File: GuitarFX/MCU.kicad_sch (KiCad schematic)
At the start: 36 parts, among them J2 USB_C_Receptacle_USB2.0, J301 Conn_ARM_SWD_TagConnect_TC2030, U2 STM32H733VGTx, U301 USBLC6-2SC6, Y301 24MHz

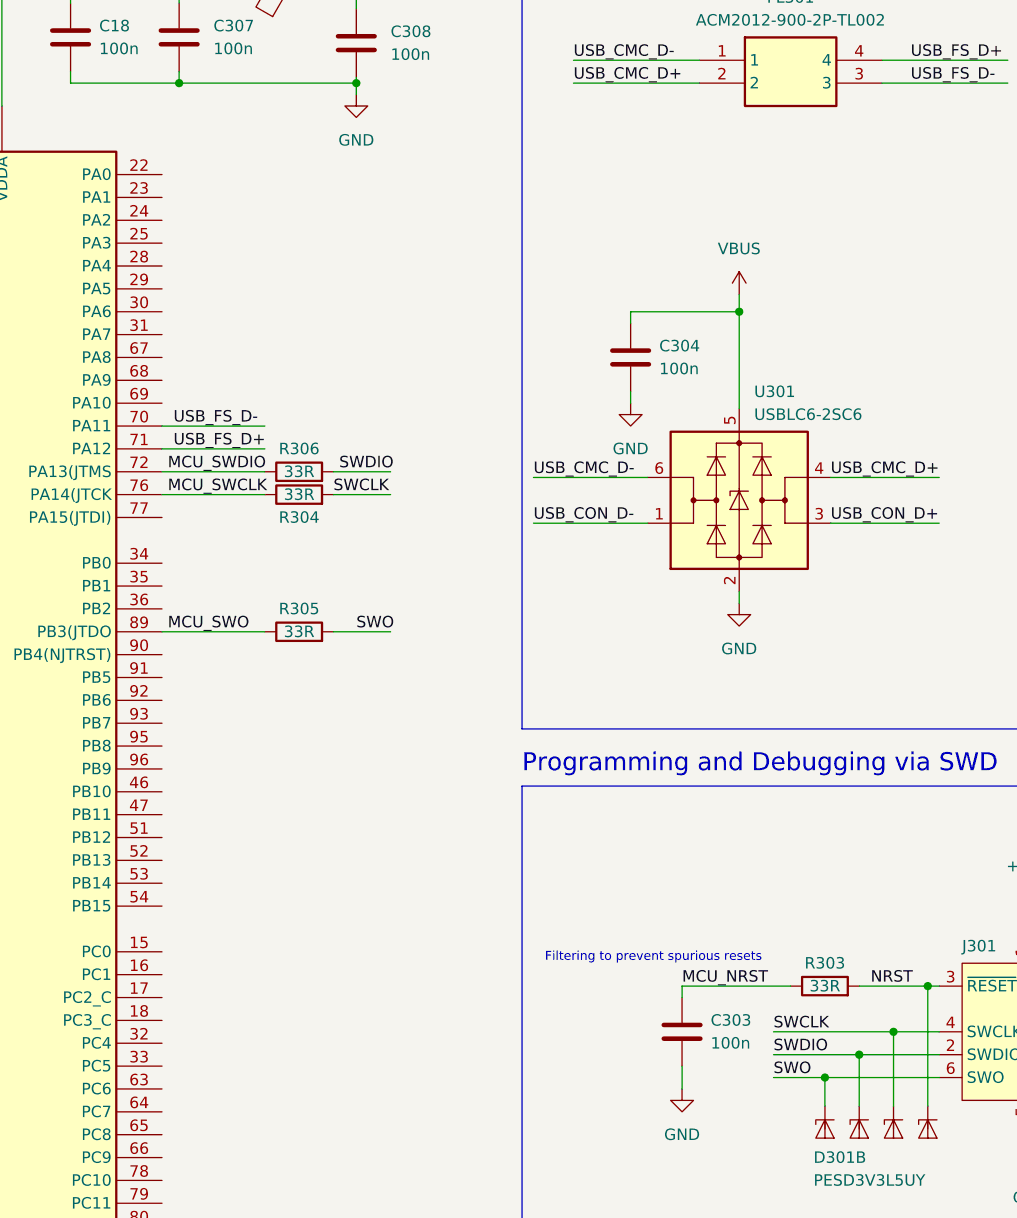
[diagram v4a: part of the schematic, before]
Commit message: Finished i2s and i2c connections on codec and mcu
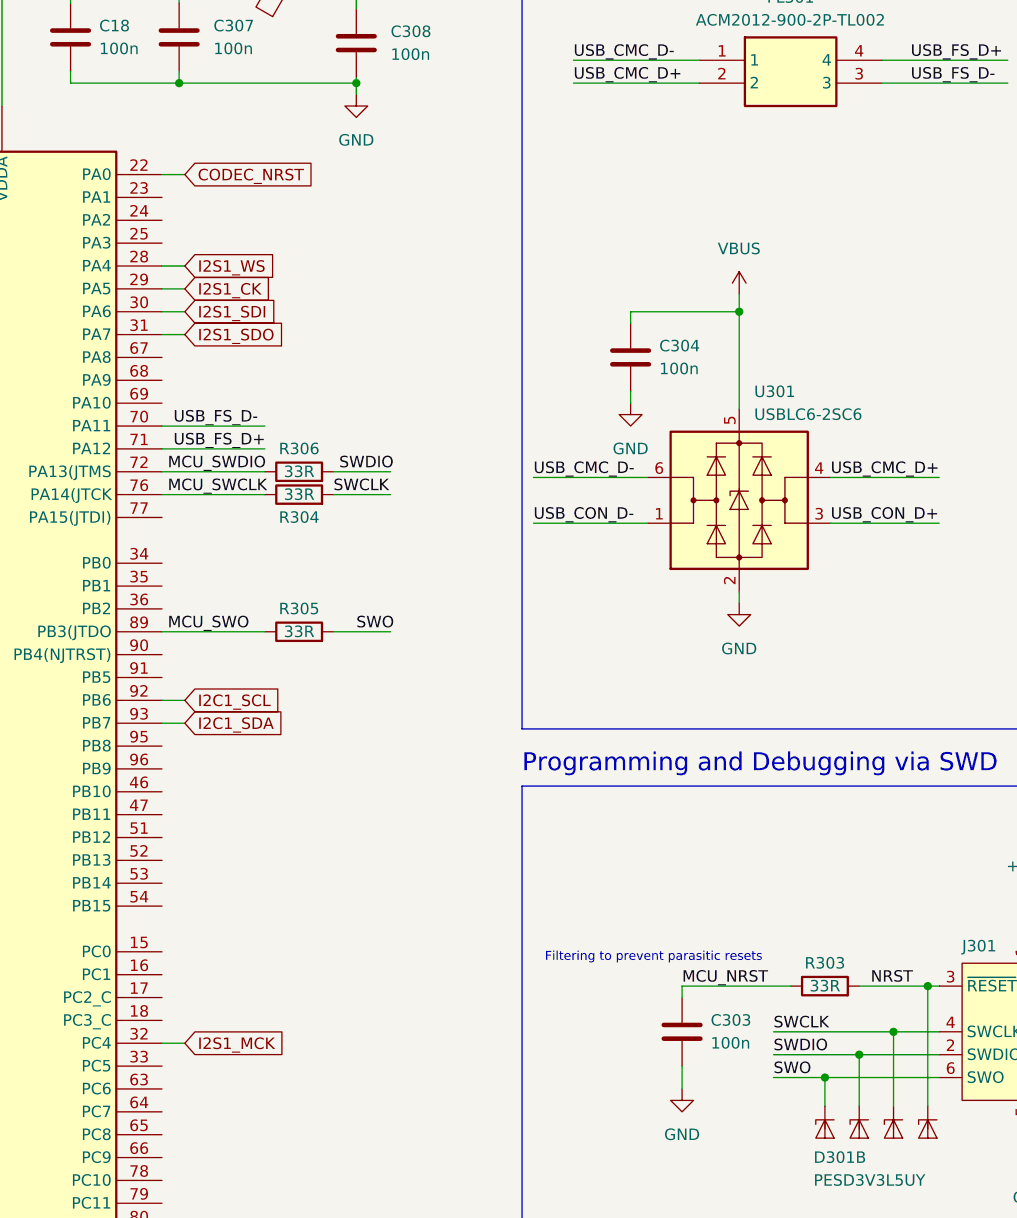
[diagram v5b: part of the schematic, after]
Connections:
- net CODEC_NRST: now reaches U2.22 (PA0)
- net I2S1_WS: now reaches U2.28 (PA4)
- net I2S1_CK: now reaches U2.29 (PA5)
- net I2S1_SDI: now reaches U2.30 (PA6)
- net I2S1_SDO: now reaches U2.31 (PA7)
- net I2S1_MCK: now reaches U2.32 (PC4)
- net I2C1_SCL: now reaches U2.92 (PB6)
- net I2C1_SDA: now reaches U2.93 (PB7)
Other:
- note added: "Filtering to prevent parasitic resets"
- note removed: "Filtering to prevent spurious resets"

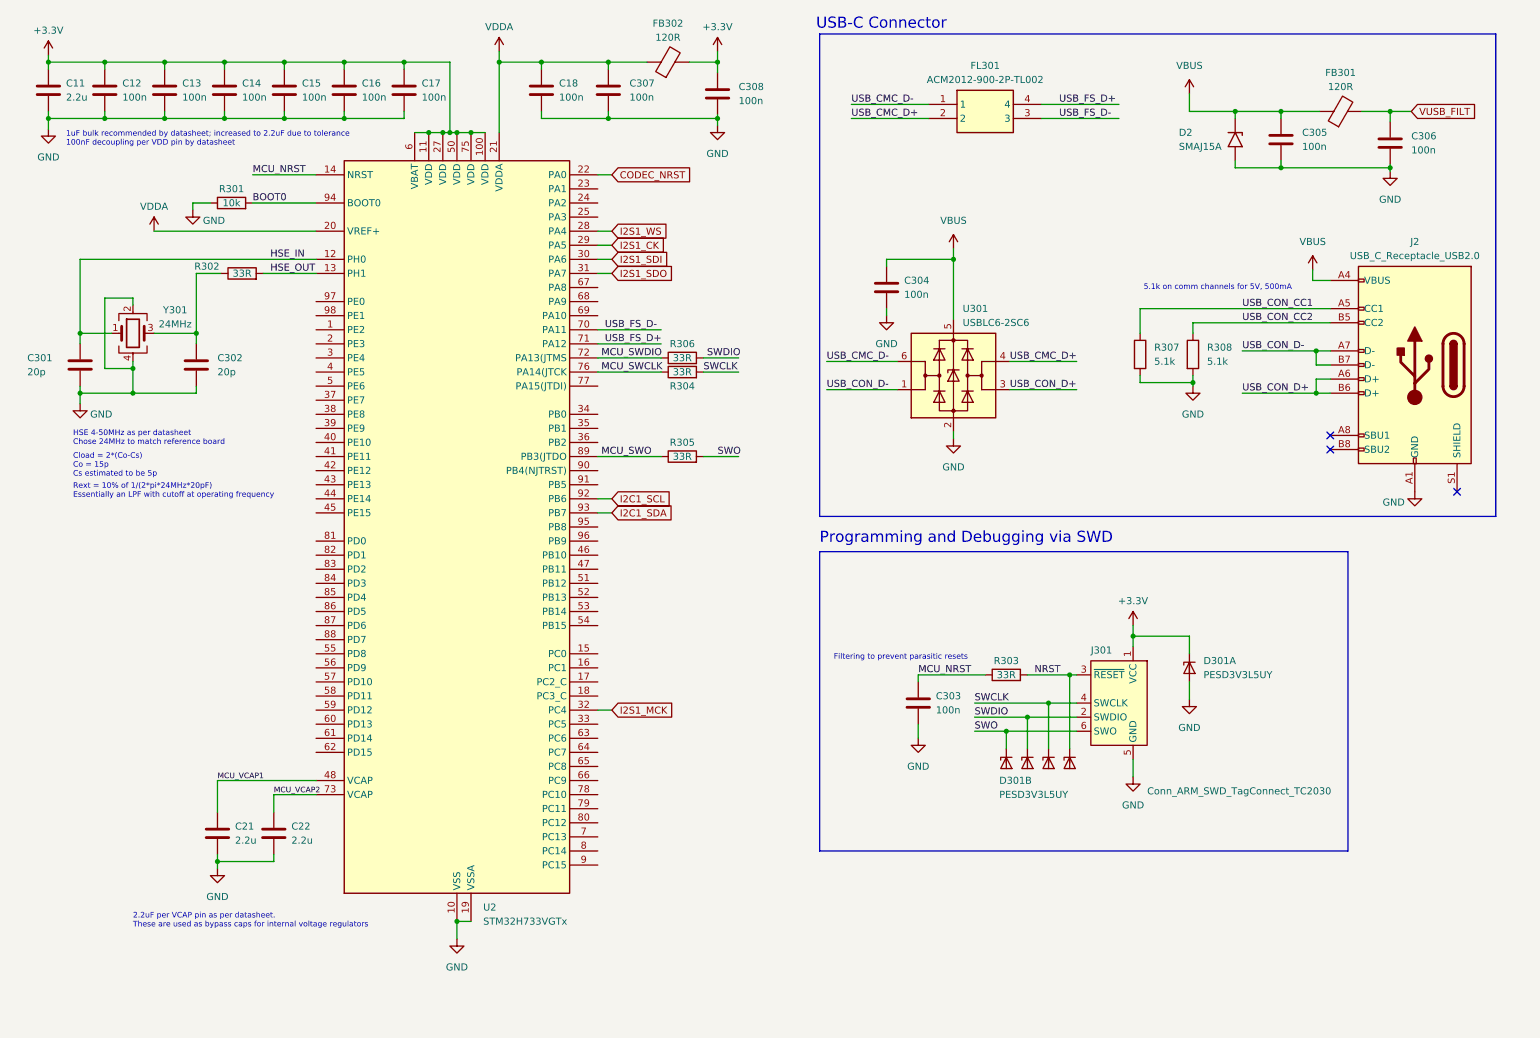
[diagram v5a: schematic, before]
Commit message: Added RGB LEDs and ADC connections for potentiometer readings along with connector
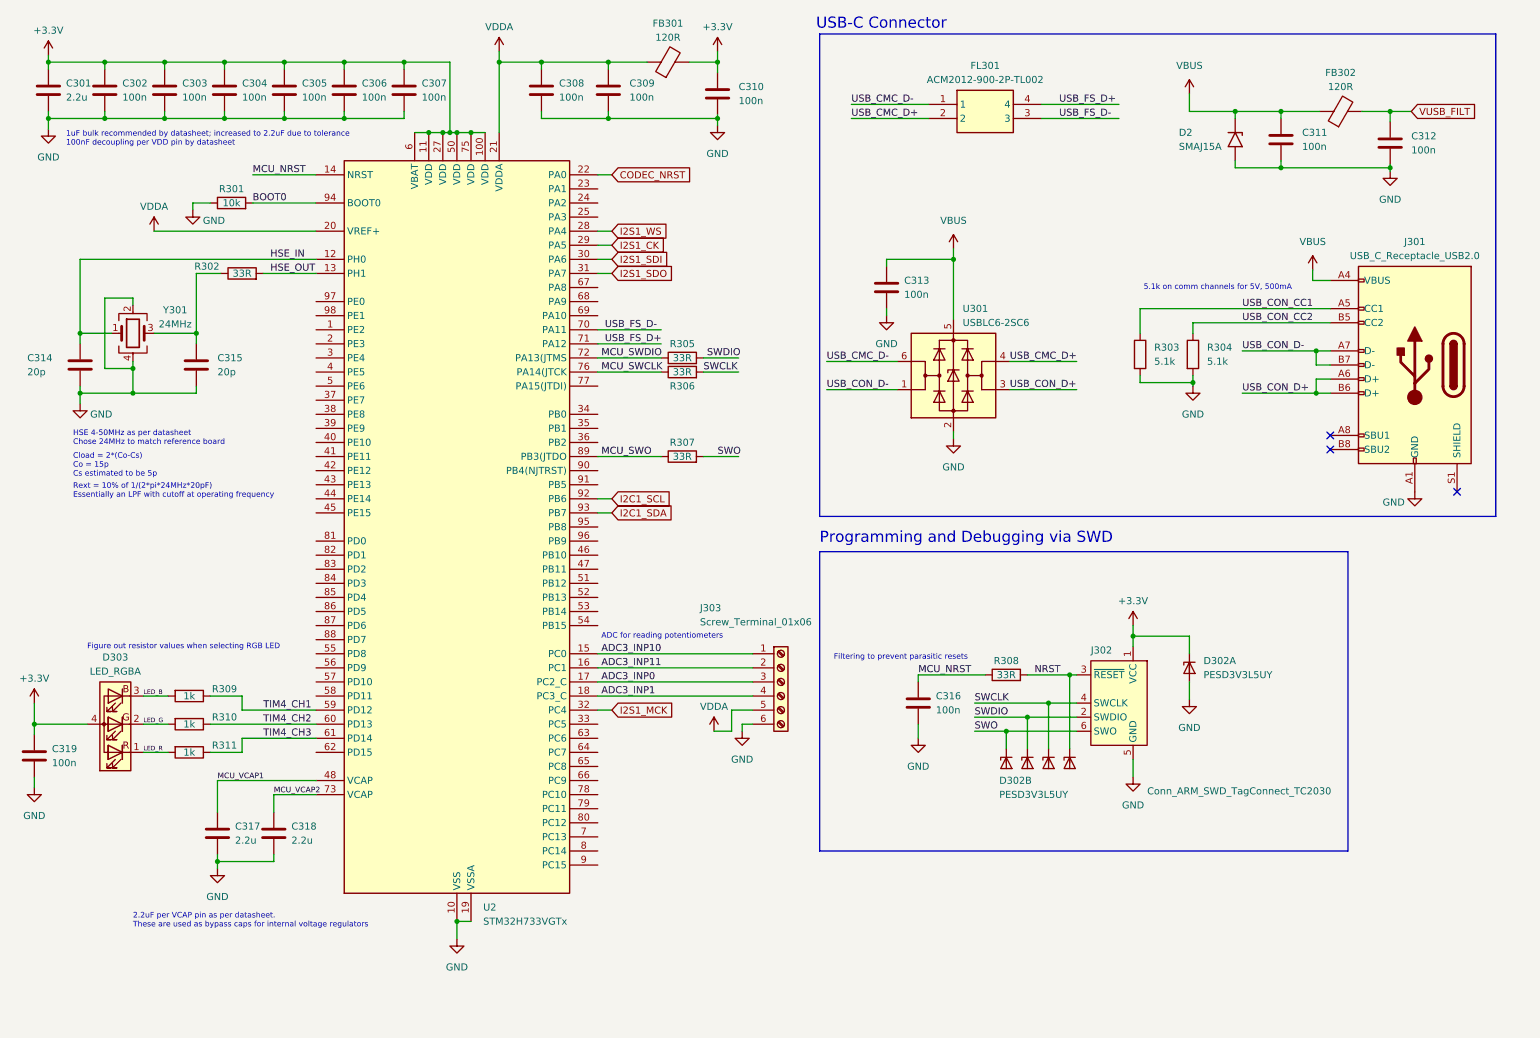
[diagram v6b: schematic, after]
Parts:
- added C319: 100n, symbol Device:C
- added D303: LED_RGBA, symbol Device:LED_RGBA
- added J303: Screw_Terminal_01x06, symbol Connector:Screw_Terminal_01x06
- added R309, R310, R311: 1k, symbol Device:R
- renumbered C11 to C301, C12 to C302, C13 to C303, C14 to C304, C15 to C305, C16 to C306, C17 to C307, C18 to C308, C307 to C309, C308 to C310, C305 to C311, C306 to C312, C304 to C313, C301 to C314, C302 to C315, C303 to C316, C21 to C317, C22 to C318, D301 to D302, FB302 to FB301, FB301 to FB302, J2 to J301, J301 to J302, R307 to R303, R308 to R304, R306 to R305, R304 to R306, R305 to R307, R303 to R308
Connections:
- net +3.3V: now also C319.1, D303.4 (A)
- net GND: now also C319.2, J303.6 (Pin_6)
- net VDDA: now also J303.5 (Pin_5)
- net ADC3_INP10: now reaches U2.15 (PC0)
- net ADC3_INP10: now also J303.1 (Pin_1)
- net ADC3_INP11: now reaches U2.16 (PC1)
- net ADC3_INP11: now also J303.2 (Pin_2)
- net ADC3_INP0: now reaches U2.17 (PC2_C)
- net ADC3_INP0: now also J303.3 (Pin_3)
- net ADC3_INP1: now reaches U2.18 (PC3_C)
- net ADC3_INP1: now also J303.4 (Pin_4)
- net TIM4_CH1: now reaches U2.59 (PD12)
- net TIM4_CH1: now also R309.1
- net TIM4_CH2: now reaches U2.60 (PD13)
- net TIM4_CH2: now also R310.1
- net TIM4_CH3: now reaches U2.61 (PD14)
- net TIM4_CH3: now also R311.1
- new net LED_B: D303.3 (BK), R309.2
- new net LED_G: D303.2 (GK), R310.2
- new net LED_R: D303.1 (RK), R311.2
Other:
- note added: "ADC for reading potentiometers"
- note added: "Figure out resistor values when selecting RGB LED"

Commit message: Got rid of most ERC violations
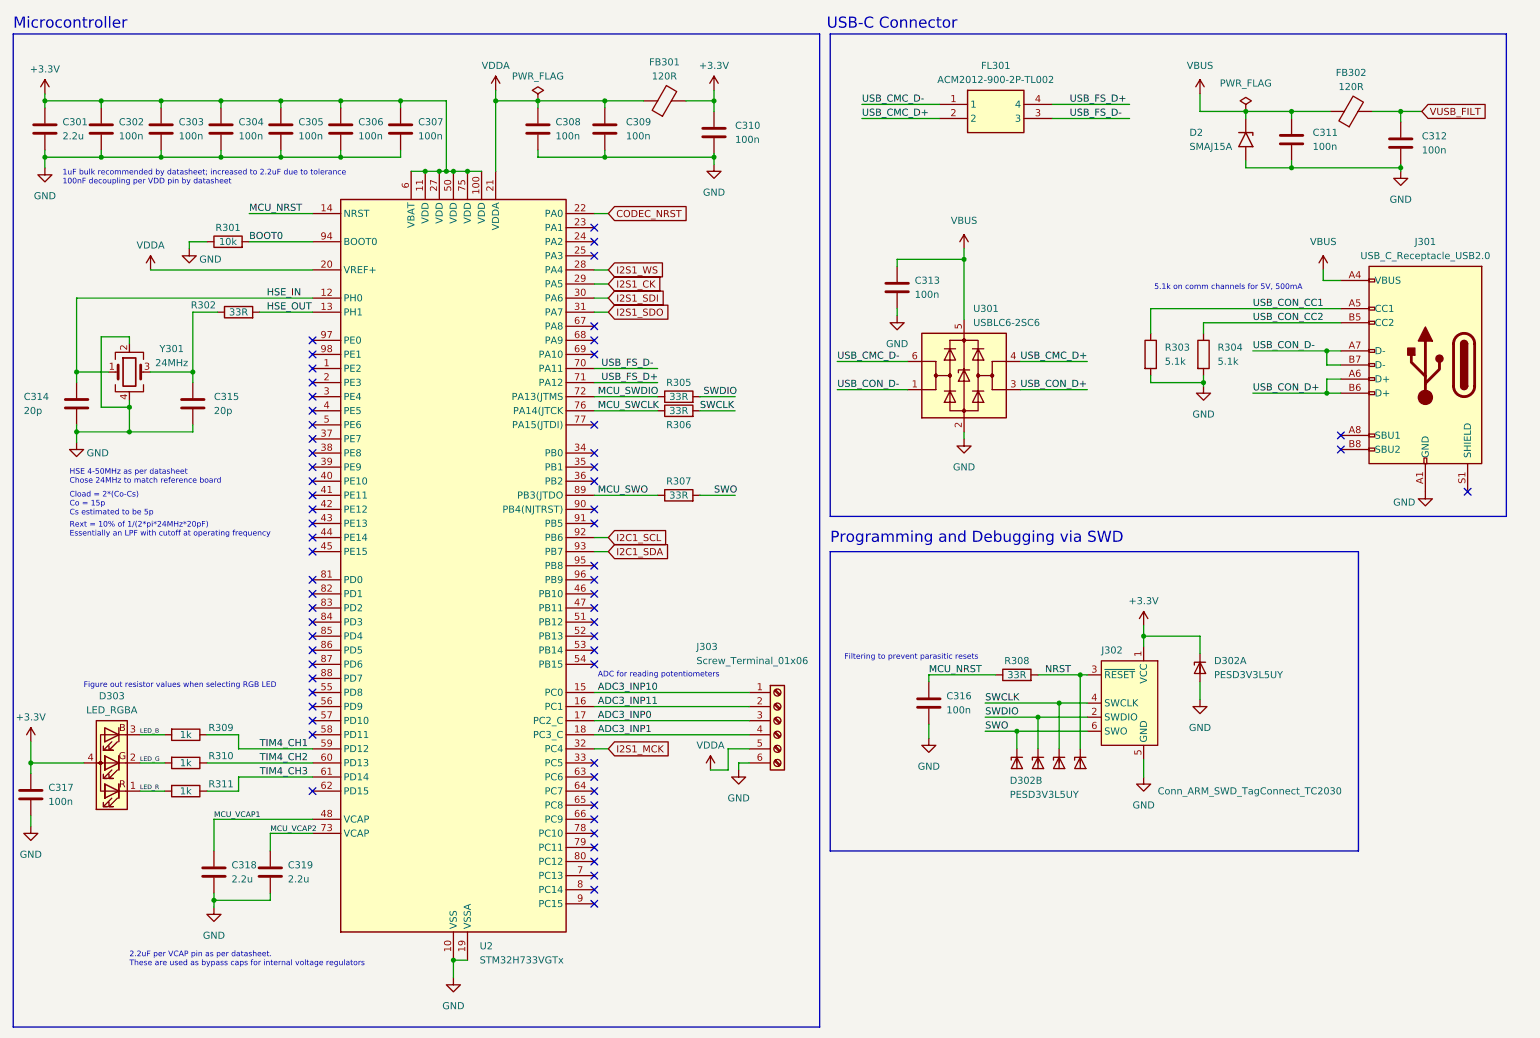
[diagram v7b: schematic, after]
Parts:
- renumbered C319 to C317, C317 to C318, C318 to C319
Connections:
- no-connect marks 3 -> 63
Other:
- note added: "Microcontroller"
- moved on the sheet: C301, C302, C303, C304, C305, C306, C307, C308, C309, C310, C311, C312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

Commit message: Updated footprints for capacitors
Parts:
- C301, C302, C318, C319: footprint (none) -> Capacitor_SMD:C_0603_1608Metric
- C303, C304, C305, C306, C307, C308, C309, C310, C311, C312, C313, C314, C315, C316, C317: footprint (none) -> Capacitor_SMD:C_0402_1005Metric
